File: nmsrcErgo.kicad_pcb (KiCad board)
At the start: 2 copper layers, 143.4 x 117.6 mm, 56 parts, among them SW1 RotaryEncoder_Switch, U1 Nice_Nano_V2

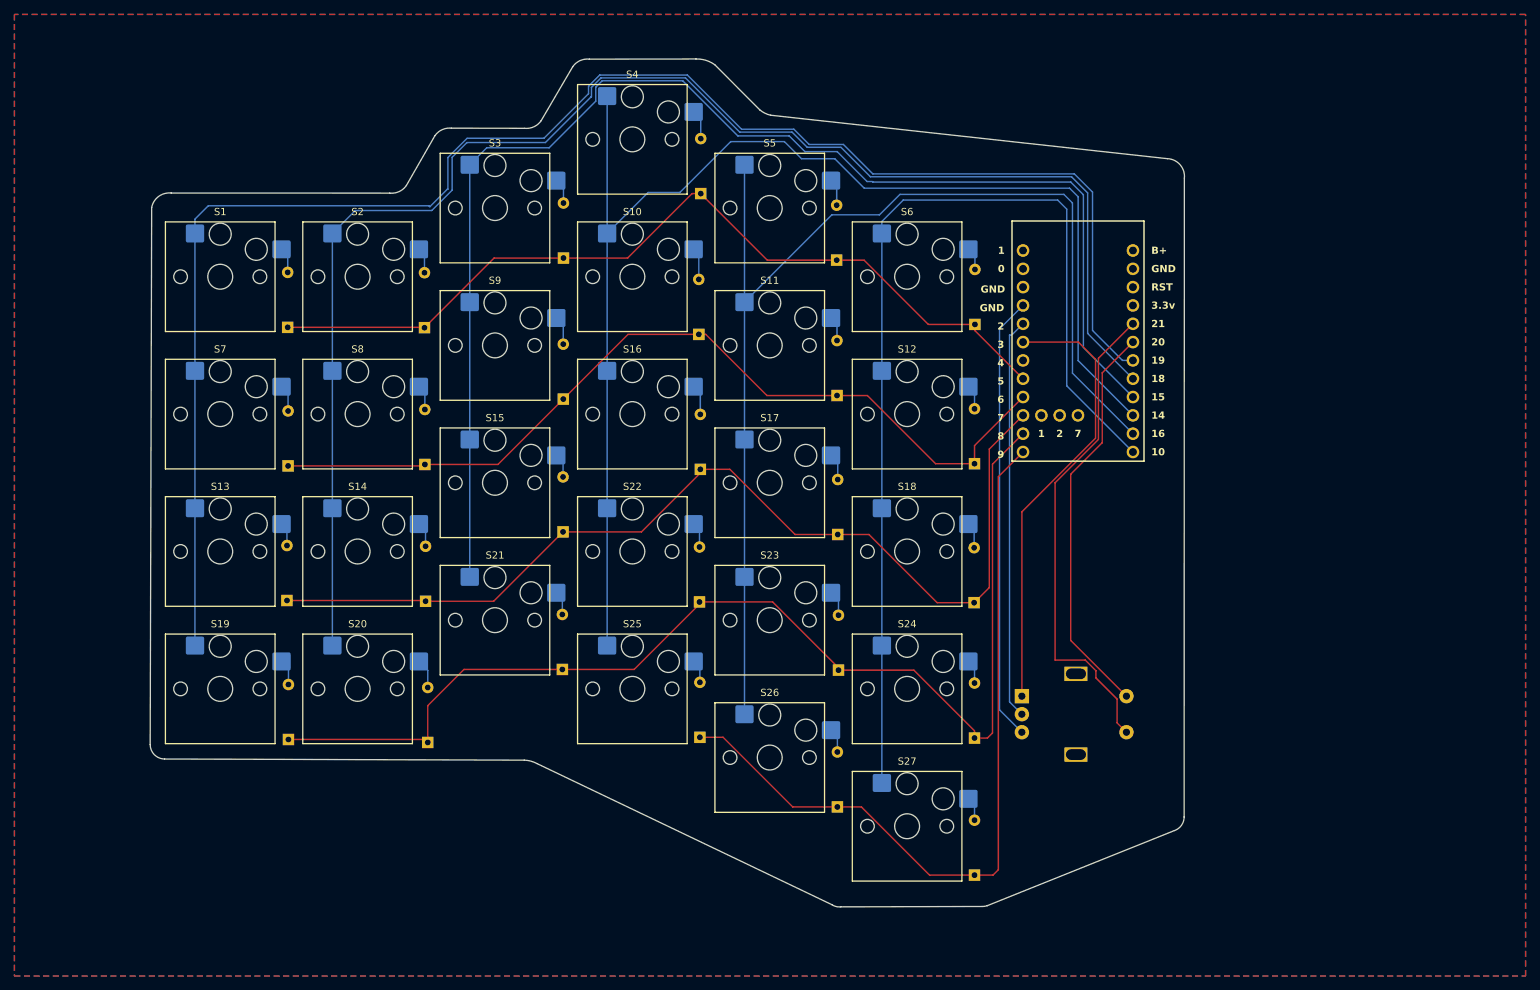
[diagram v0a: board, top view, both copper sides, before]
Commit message: changed some keys orientation
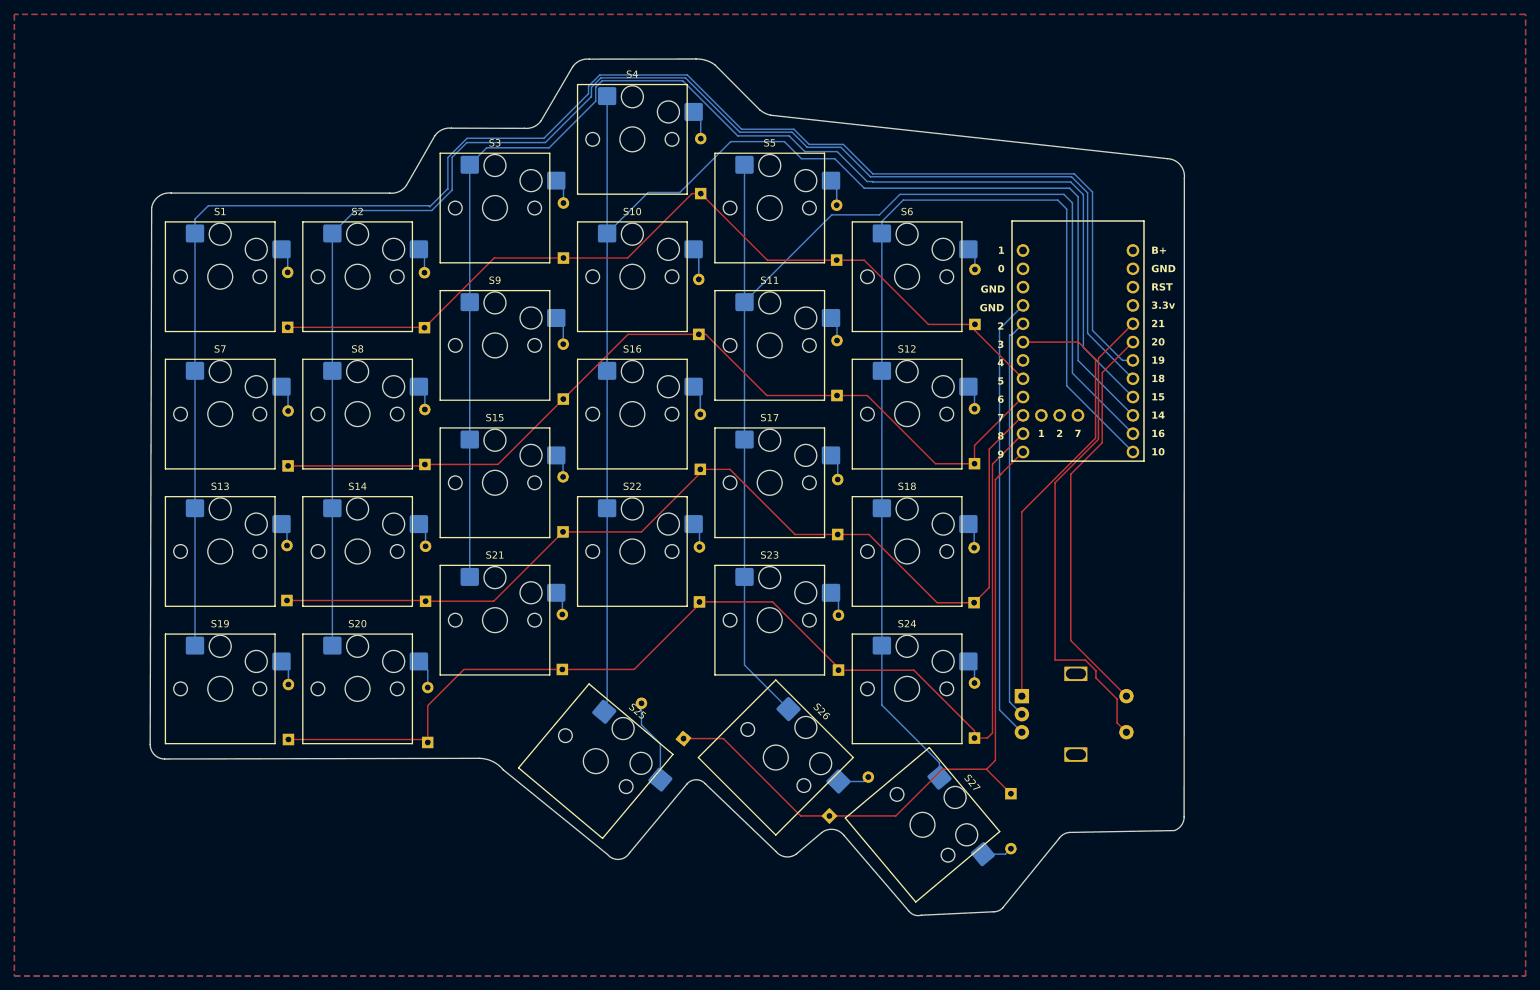
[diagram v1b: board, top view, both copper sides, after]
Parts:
- moved D27 12.4 mm to (165.7, 139.4), turned to -90 degrees
- moved S25 11.2 mm to (108.1, 134.8), turned to -40 degrees
- moved D25 2.27 mm to (120.3, 131.7), turned to 140 degrees
- moved S27 2.15 mm to (153.4, 143.7), turned to -50 degrees
- moved D26 1.66 mm to (140.5, 142.4), turned to 45 degrees
- moved S26 0.84 mm to (133.1, 134.3), turned to -45 degrees
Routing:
- net Column 3: track 183.4 -> 192.8 mm
- net Net-(D25-A): track 3.25 -> 11.7 mm
- net Row 4: track 109.0 -> 100.9 mm
- net Column 5: track 142.7 -> 145.3 mm
- net Column 4: track 164.3 -> 166.1 mm
- net Net-(D26-A): track 3.40 -> 4.39 mm
- net Net-(D27-A): track 3.31 -> 4.20 mm
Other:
- board size 143.4 x 117.6 mm -> 143.4 x 118.8 mm

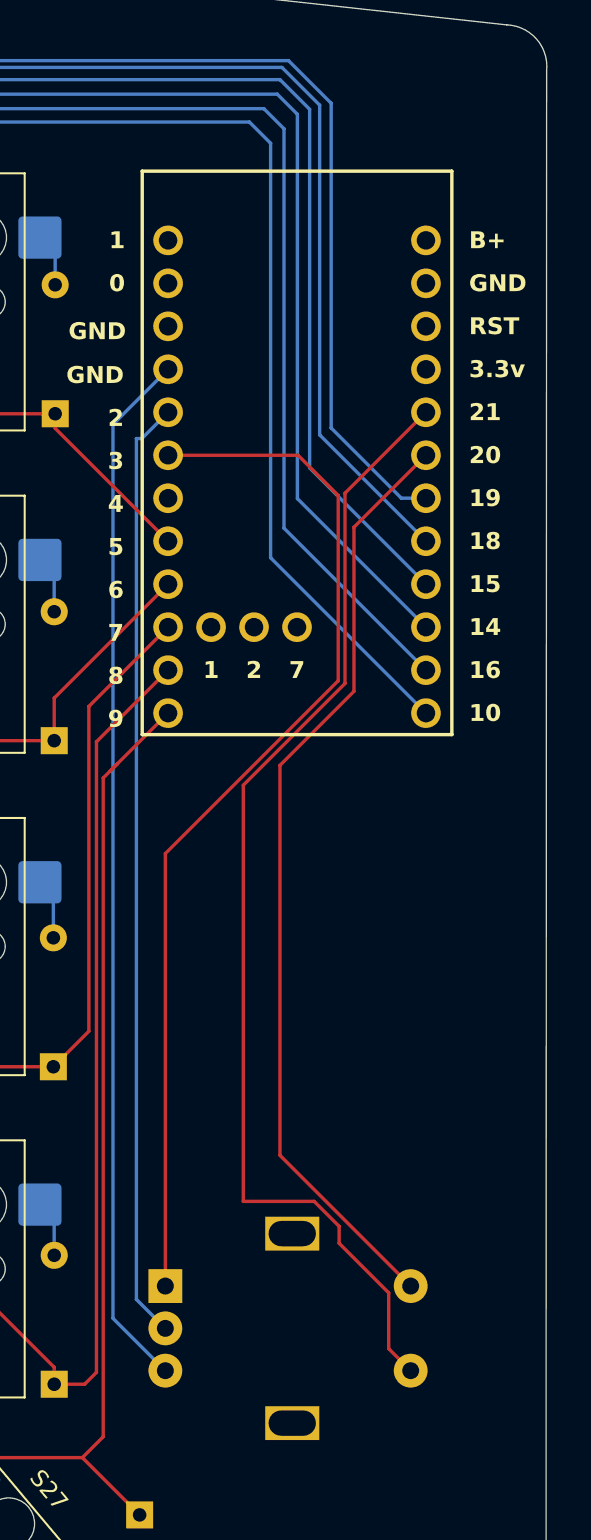
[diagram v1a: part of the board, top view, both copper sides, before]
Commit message: on/off switch and fixed encoder. added battery solder pads
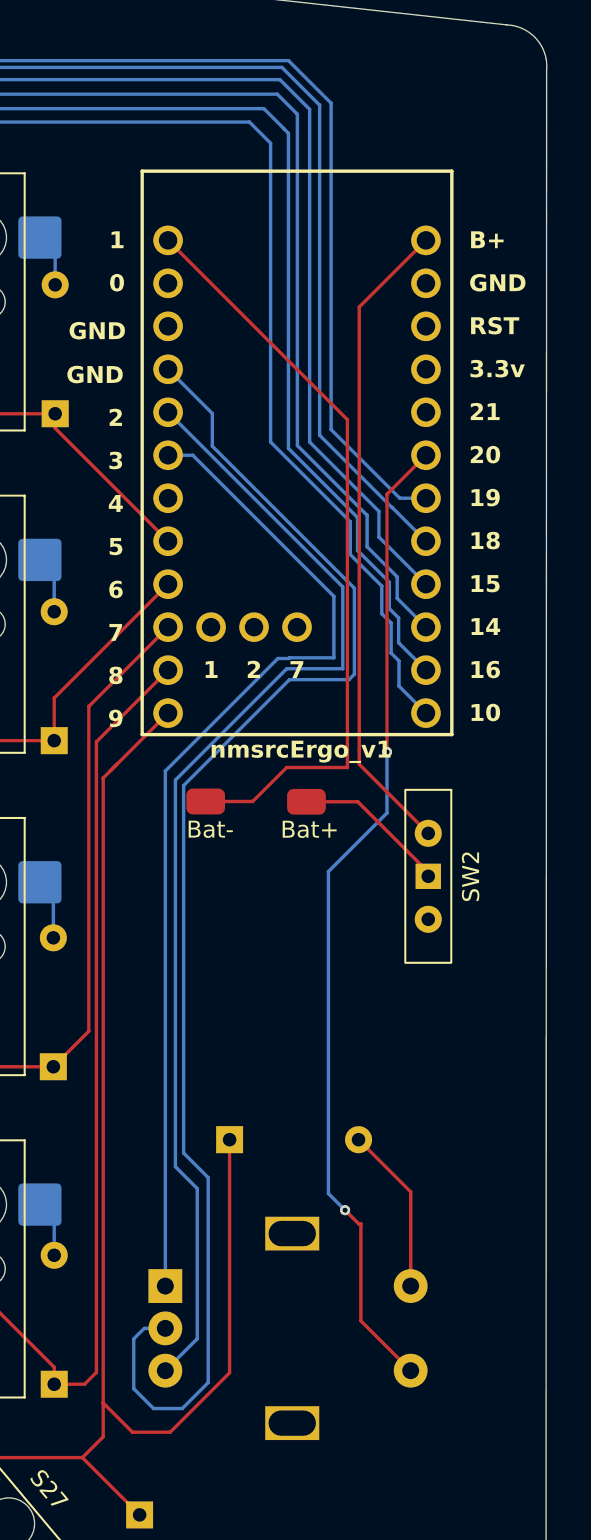
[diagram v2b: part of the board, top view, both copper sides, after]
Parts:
- added Bat+: SolderJumper_2_Bridged, ScottoKeebs_Miscellaneous:solderpadv2, F.Cu at (175.5, 97.2)
- added Bat-: SolderJumper_2_Bridged, ScottoKeebs_Miscellaneous:solderpadv2, F.Cu at (169.6, 97.2)
- added D28: Diode, ScottoKeebs_Components:Diode_DO-35, B.Cu at (171.0, 117.2)
- added SW2: SW_Slide_DPDT, Button_Switch_THT:SW_Slide-03_Wuerth-WS-SLTV_10x2.5x6.4_P2.54mm, F.Cu at (182.7, 101.6)
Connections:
- SW1 pad S1: Row 5 -> Column 6
- SW1 pad S2: Row 6 -> Net-(D28-A)
- U1 pad 1: unconnected-(U1-Pad1) -> Bat-
- U1 pad 19: Row 6 -> Column 6
- U1 pad 20: Row 5 -> unconnected-(U1-21-Pad20)
- U1 pad 24: unconnected-(U1-B+-Pad24) -> Bat+
- U1 pad 4: Row 9 -> Row 8
- U1 pad 5: Row 8 -> Row 9
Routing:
- net Row 5: track 67.7 -> 0.00 mm
- net Column 6: track 0.00 -> 58.6 mm, vias 0 -> 2
- net Row 6: track 55.9 -> 0.00 mm
- net Bat-: track 0.00 -> 44.8 mm
- net Bat+: track 0.00 -> 38.4 mm
- net Row 8: track 55.8 -> 81.9 mm
- net Row 4: track 100.9 -> 124.3 mm
- net Net-(D28-A): track 0.00 -> 9.93 mm
- net Net-(JP1-A): track 0.00 -> 9.17 mm
- net Row 9: track 61.8 -> 68.3 mm
- net Row 7: track 62.0 -> 60.1 mm
